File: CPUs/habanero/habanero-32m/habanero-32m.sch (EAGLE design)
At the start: 38 parts, among them IC1 PIC32MX564F128H-80I/PT

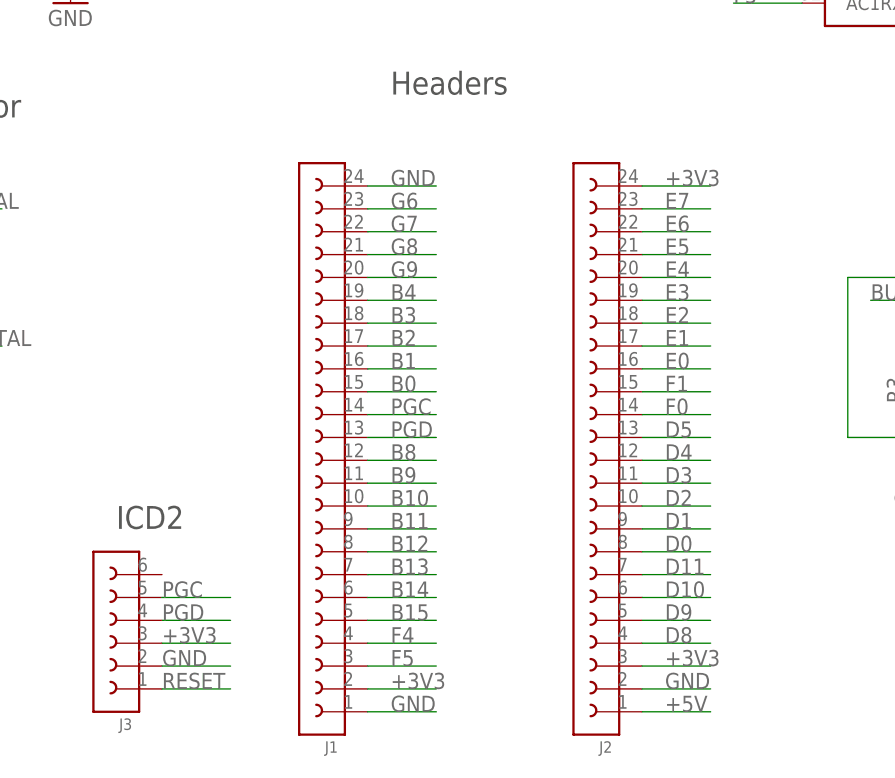
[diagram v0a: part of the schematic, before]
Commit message: modificaciones en esquematico
- se cambiaron los pin headers de 24 a 23 posiciones, para dejar mas
espacio libre al conector usb on-the-go,
- se corrigio un error de conexion en el conector para el pickit3
-se generaron nuevos modelos ya con pin headers
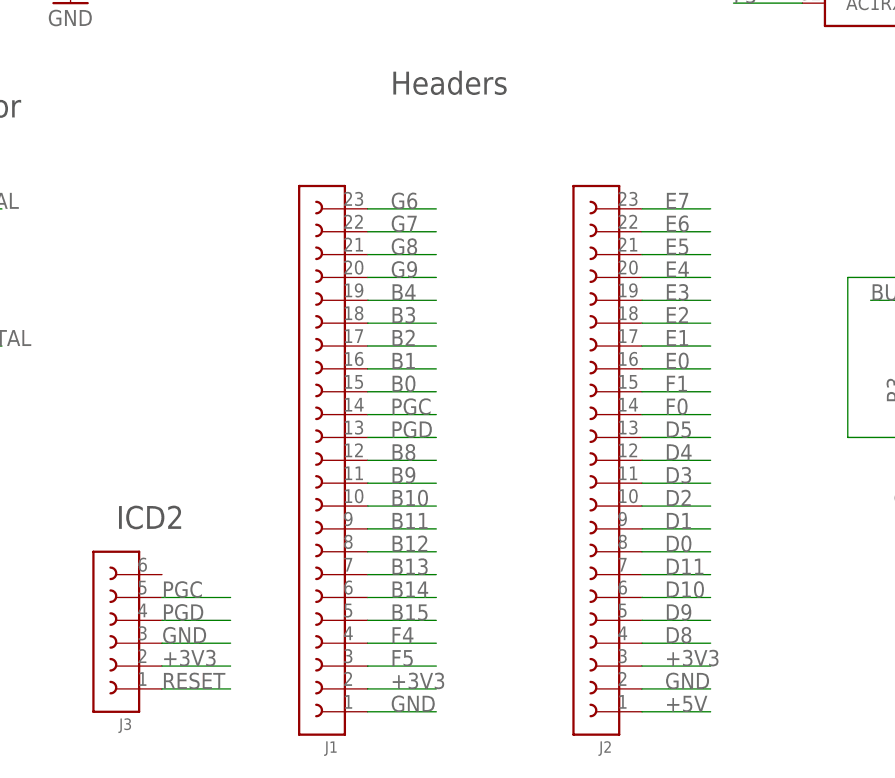
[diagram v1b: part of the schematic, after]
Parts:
- J1, J2: device wurth-pin-socket-headers:61302411121 -> wurth-pin-socket-headers:61302311121
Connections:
- net +3V3: now also J3.2; no longer J2.24, J3.3
- net GND: now also J3.3; no longer J1.24, J3.2
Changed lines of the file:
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@@
 <?xml version="1.0" encoding="utf-8"?>
 <!DOCTYPE eagle SYSTEM "eagle.dtd">
-<eagle version="6.2">
+<eagle version="6.4">
 <drawing>
 <settings>
@@
 </part>
 <part name="GND5" library="supply" deviceset="GND" device=""/>
-<part name="J1" library="wurth-pin-socket-headers" deviceset="6130241?" device="1121"/>
-<part name="J2" library="wurth-pin-socket-headers" deviceset="6130241?" device="1121"/>
+<part name="J1" library="wurth-pin-socket-headers" deviceset="6130231?" device="1121"/>
+<part name="J2" library="wurth-pin-socket-headers" deviceset="6130231?" device="1121"/>
 </parts>
 <sheets>
@@
 <instance part="C16" gate="G$1" x="187.96" y="78.74"/>
 <instance part="GND5" gate="1" x="187.96" y="68.58"/>
-<instance part="J1" gate="G$1" x="76.2" y="48.26" rot="R180"/>
-<instance part="J2" gate="G$1" x="106.68" y="48.26" rot="R180"/>
+<instance part="J1" gate="G$1" x="76.2" y="45.72" rot="R180"/>
+<instance part="J2" gate="G$1" x="106.68" y="45.72" rot="R180"/>
 </instances>
 <busses>
@@
 </segment>
 <segment>
-<wire x1="58.42" y1="20.32" x2="66.04" y2="20.32" width="0.1524" layer="91"/>
-<label x="58.42" y="20.32" size="1.778" layer="95"/>
-<pinref part="J3" gate="G$1" pin="2"/>
-</segment>
-<segment>
 <wire x1="81.28" y1="15.24" x2="88.9" y2="15.24" width="0.1524" layer="91"/>
 <label x="83.82" y="15.24" size="1.778" layer="95"/>
@@
 </segment>
 <segment>
-<wire x1="81.28" y1="73.66" x2="88.9" y2="73.66" width="0.1524" layer="91"/>
-<label x="83.82" y="73.66" size="1.778" layer="95"/>
-<pinref part="J1" gate="G$1" pin="24"/>
-</segment>
-<segment>
 <pinref part="C16" gate="G$1" pin="2"/>
 <wire x1="187.96" y1="73.66" x2="187.96" y2="71.12" width="0.1524" layer="91"/>
 <pinref part="GND5" gate="1" pin="GND"/>
+</segment>
+<segment>
+<wire x1="58.42" y1="22.86" x2="66.04" y2="22.86" width="0.1524" layer="91"/>
+<label x="58.42" y="22.86" size="1.778" layer="95"/>
+<pinref part="J3" gate="G$1" pin="3"/>
 </segment>
 </net>
@@
 <pinref part="C9" gate="G$1" pin="1"/>
 <pinref part="IC4" gate="G$1" pin="C+"/>
-</segment>
-<segment>
-<wire x1="58.42" y1="22.86" x2="66.04" y2="22.86" width="0.1524" layer="91"/>
-<label x="58.42" y="22.86" size="1.778" layer="95"/>
-<pinref part="J3" gate="G$1" pin="3"/>
 </segment>
 <segment>
@@
 </segment>
 <segment>
-<wire x1="111.76" y1="73.66" x2="119.38" y2="73.66" width="0.1524" layer="91"/>
-<label x="114.3" y="73.66" size="1.778" layer="95"/>
-<pinref part="J2" gate="G$1" pin="24"/>
-</segment>
-</net>
+<wire x1="58.42" y1="20.32" x2="66.04" y2="20.32" width="0.1524" layer="91"/>
+<label x="58.42" y="20.32" size="1.778" layer="95"/>
+<pinref part="J3" gate="G$1" pin="2"/>
+</segment>
+</net>

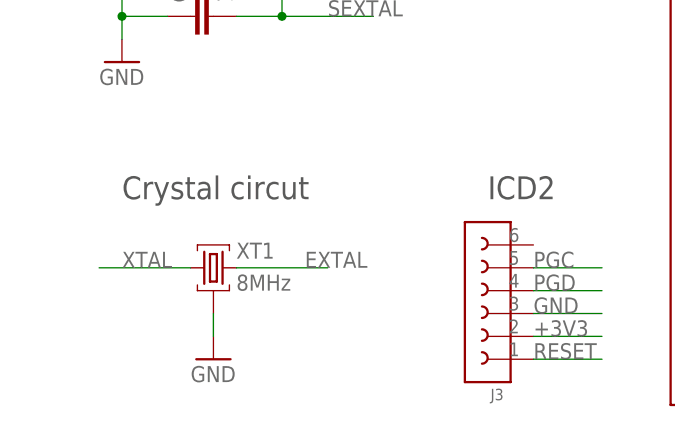
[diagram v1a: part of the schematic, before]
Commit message: modify resonator part
unrute all
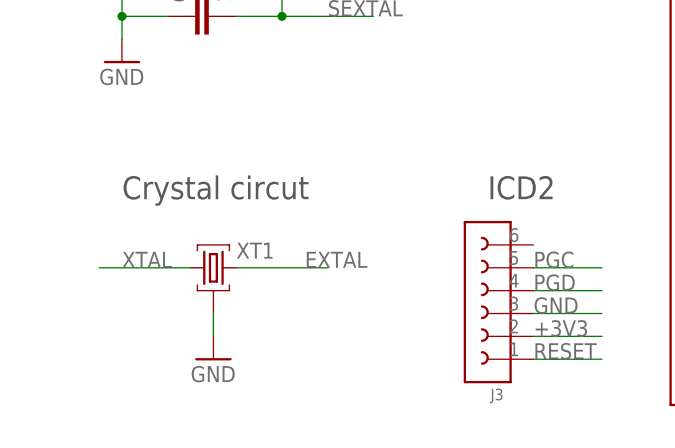
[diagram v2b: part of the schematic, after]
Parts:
- XT1: value 8MHz -> (none); device abracon-resonators:AWSCR-8.00MGD-C -> abracon-resonators:AWSCR-12.00CR-C
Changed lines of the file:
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@@
 <setting verticaltext="up"/>
 </settings>
-<grid distance="0.1" unitdist="inch" unit="inch" style="lines" multiple="1" display="yes" altdistance="0.01" altunitdist="inch" altunit="inch"/>
+<grid distance="0.1" unitdist="inch" unit="inch" style="lines" multiple="1" display="no" altdistance="0.01" altunitdist="inch" altunit="inch"/>
 <layers>
 <layer number="1" name="Top" color="4" fill="1" visible="no" active="no"/>
@@
 <part name="GND21" library="supply" deviceset="GND" device=""/>
 <part name="J3" library="wurth-pin-socket-headers" deviceset="6130061?" device="1121"/>
-<part name="XT1" library="abracon-resonators" deviceset="AWSCR-*MGD-C" device="" technology="8.00" value="8MHz"/>
 <part name="XT2" library="abracon-crystals" deviceset="ABS07-120-32.768KHZ-T" device="" value="32.768"/>
 <part name="SW1" library="esw-tactile-sw" deviceset="TL3301?*J" device="N" technology="F160Q"/>
@@
 <part name="J1" library="wurth-pin-socket-headers" deviceset="6130231?" device="1121"/>
 <part name="J2" library="wurth-pin-socket-headers" deviceset="6130231?" device="1121"/>
+<part name="XT1" library="abracon-resonators" deviceset="AWSCR-*CR-C" device="" technology="12.00"/>
 </parts>
 <sheets>
@@
 <instance part="GND21" gate="1" x="22.86" y="17.78"/>
 <instance part="J3" gate="G$1" x="53.34" y="25.4" rot="R180"/>
-<instance part="XT1" gate="G$1" x="22.86" y="27.94"/>
 <instance part="XT2" gate="G$1" x="30.48" y="63.5" rot="R90"/>
 <instance part="SW1" gate="G$1" x="10.16" y="109.22"/>
@@
 <instance part="J1" gate="G$1" x="76.2" y="45.72" rot="R180"/>
 <instance part="J2" gate="G$1" x="106.68" y="45.72" rot="R180"/>
+<instance part="XT1" gate="G$1" x="22.86" y="27.94"/>
 </instances>
 <busses>
